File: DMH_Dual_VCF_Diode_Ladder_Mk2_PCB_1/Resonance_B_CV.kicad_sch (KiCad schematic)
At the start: 26 parts, among them J22 Conn_01x06_PinHeader, Q3 BC548, Q4 BC548, SW8 SW_DPDT_x2, U2 TL074

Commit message: Corrected pin header footprint assignments
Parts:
- J22: footprint Connector_PinHeader_2.54mm:PinHeader_1x10_P2.54mm_Vertical -> Connector_PinHeader_2.54mm:PinHeader_1x06_P2.54mm_Vertical
- J22: footprint (none) -> Connector_PinHeader_2.54mm:PinHeader_1x06_P2.54mm_Vertical
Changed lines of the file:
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@@
 			)
 		)
-		(property "Footprint" "Connector_PinHeader_2.54mm:PinHeader_1x10_P2.54mm_Vertical"
+		(property "Footprint" "Connector_PinHeader_2.54mm:PinHeader_1x06_P2.54mm_Vertical"
 			(at 76.2 100.33 0)
 			(effects
@@
 			)
 		)
-		(property "Footprint" ""
+		(property "Footprint" "Connector_PinHeader_2.54mm:PinHeader_1x06_P2.54mm_Vertical"
 			(at 170.18 132.08 0)
 			(effects
@@
 			)
 		)
-		(property "Footprint" ""
+		(property "Footprint" "Connector_PinHeader_2.54mm:PinHeader_1x06_P2.54mm_Vertical"
 			(at 165.1 113.03 0)
 			(effects
@@
 			)
 		)
-		(property "Footprint" "Connector_PinHeader_2.54mm:PinHeader_1x10_P2.54mm_Vertical"
+		(property "Footprint" "Connector_PinHeader_2.54mm:PinHeader_1x06_P2.54mm_Vertical"
 			(at 63.5 81.28 0)
 			(effects
@@
 			)
 		)
-		(property "Footprint" ""
+		(property "Footprint" "Connector_PinHeader_2.54mm:PinHeader_1x06_P2.54mm_Vertical"
 			(at 185.42 132.08 0)
 			(effects
@@
 			)
 		)
-		(property "Footprint" "Connector_PinHeader_2.54mm:PinHeader_1x10_P2.54mm_Vertical"
+		(property "Footprint" "Connector_PinHeader_2.54mm:PinHeader_1x06_P2.54mm_Vertical"
 			(at 110.49 129.54 0)
 			(effects

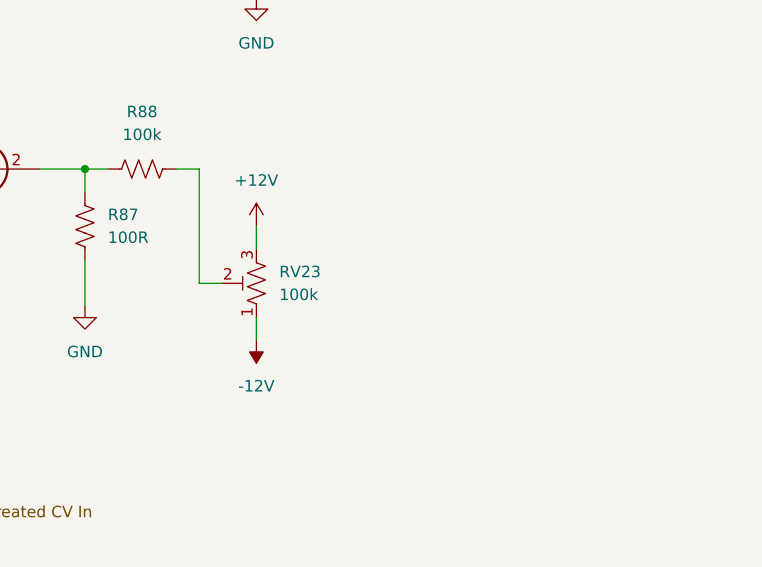
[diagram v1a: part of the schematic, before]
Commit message: Added trim pot functions to silkscreen
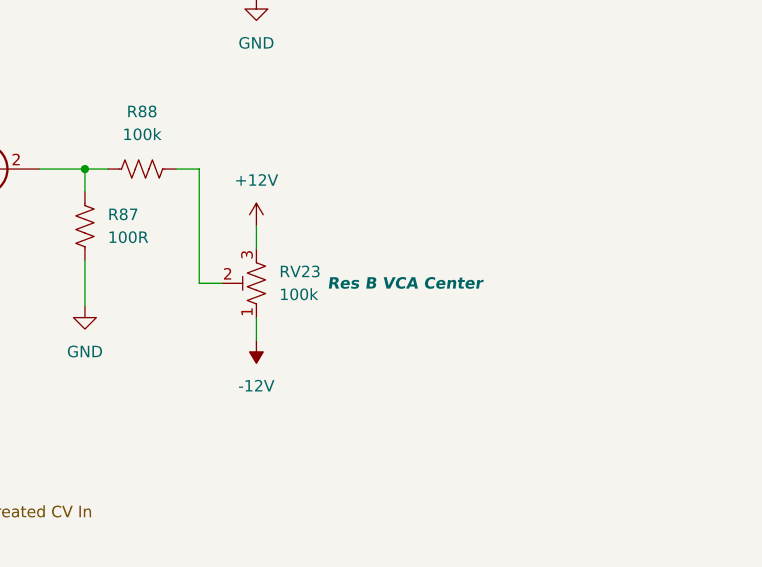
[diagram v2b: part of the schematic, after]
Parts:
- RV23: Function (none) -> Res B VCA Center
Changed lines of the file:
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@@
 		(on_board yes)
 		(dnp no)
-		(fields_autoplaced yes)
 		(property "Reference" "RV23"
 			(at 224.79 100.3299 0)
@@
 			)
 		)
+		(property "Function" "Res B VCA Center"
+			(at 238.76 101.6 0)
+			(effects
+				(font
+					(size 1.27 1.27)
+					(thickness 0.254)
+					(bold yes)
+					(italic yes)
+				)
+			)
+		)

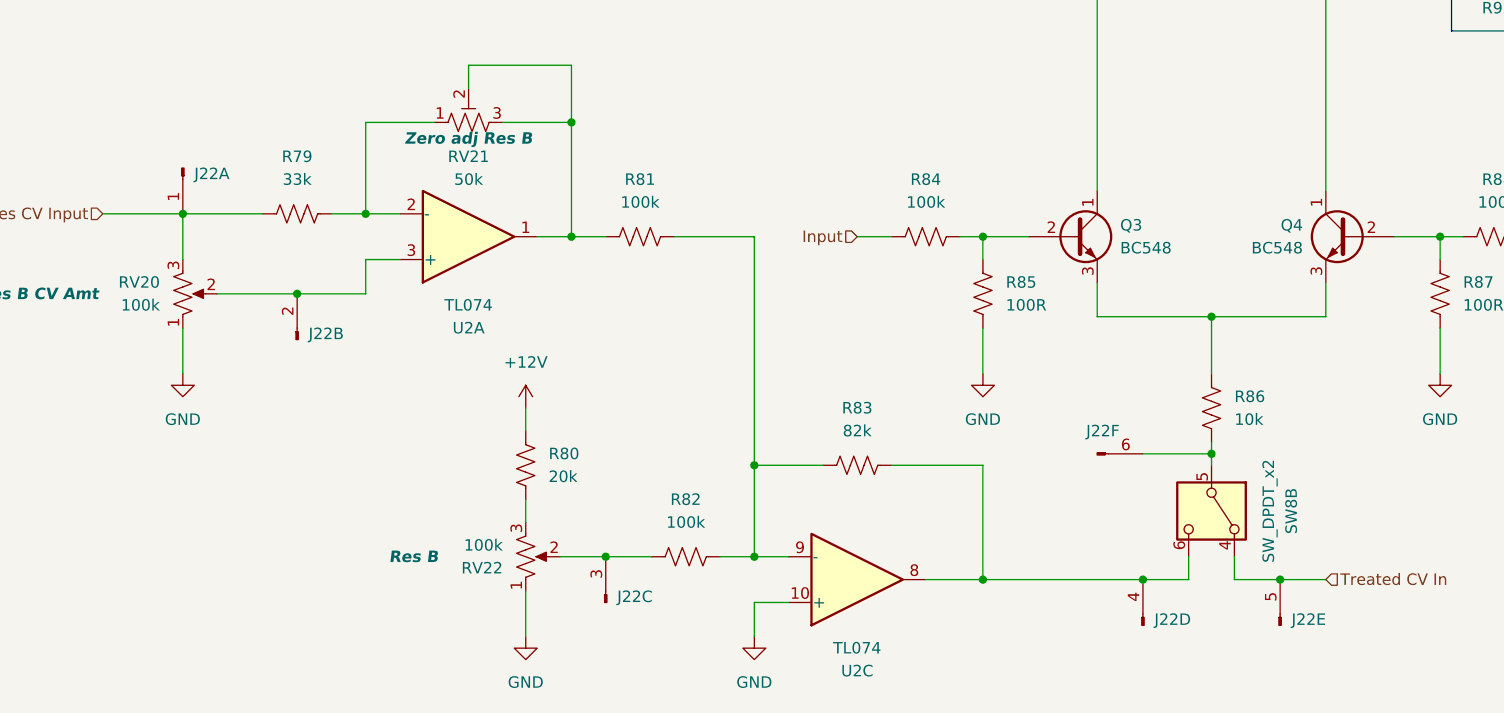
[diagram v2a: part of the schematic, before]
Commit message: Adjusted pin header connections
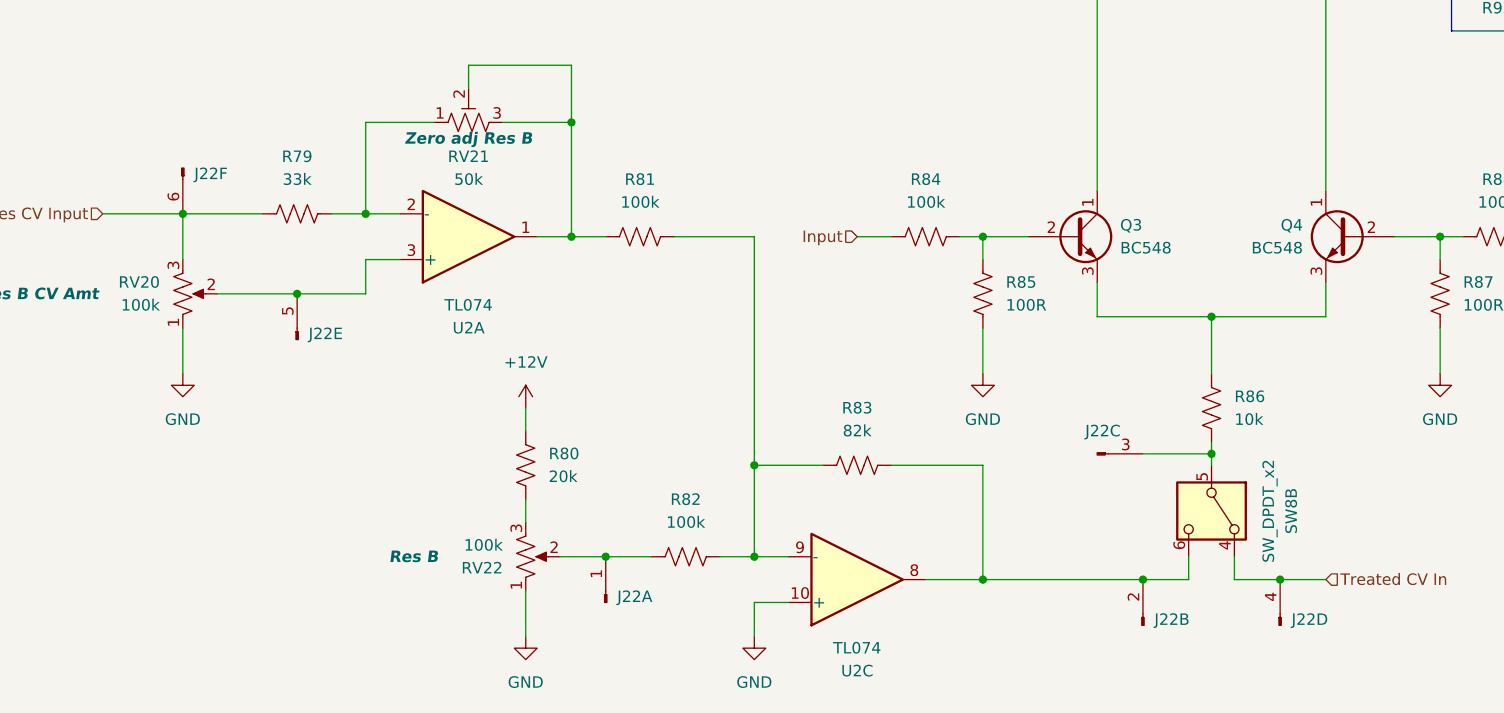
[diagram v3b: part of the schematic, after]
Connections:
- net Res CV Input: now also J22.6 (Pin_6); no longer J22.1 (Pin_1)
- net Treated CV In: now also J22.4 (Pin_4); no longer J22.5 (Pin_5)
- net at RV20.2, U2.3 (+): now also J22.5 (Pin_5); no longer J22.2 (Pin_2)
- net at R86.1, SW8.5 (B): now also J22.3 (Pin_3); no longer J22.6 (Pin_6)
- net at R83.2, SW8.6 (C), U2.8: now also J22.2 (Pin_2); no longer J22.4 (Pin_4)
- net at R82.1, RV22.2: now also J22.1 (Pin_1); no longer J22.3 (Pin_3)
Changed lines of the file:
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@@
 		(lib_id "SynthStuff:Conn_01x06_PinHeader")
 		(at 76.2 100.33 90)
-		(unit 2)
+		(unit 5)
 		(exclude_from_sim no)
 		(in_bom yes)
@@
 				(path "/58f4306d-5387-4983-bb08-41a2313fd315/f0045393-e1d0-4de8-baba-b9053cd8a11d"
 					(reference "J22")
-					(unit 2)
+					(unit 5)
 				)
 			)
@@
 		(lib_id "SynthStuff:Conn_01x06_PinHeader")
 		(at 170.18 132.08 90)
-		(unit 4)
+		(unit 2)
 		(exclude_from_sim no)
 		(in_bom yes)
@@
 			)
 		)
+		(property "Function" ""
+			(at 170.18 132.08 0)
+			(effects
+				(font
+					(size 1.27 1.27)
+				)
+			)
+		)
 		(pin "2"
 		)
@@
 				(path "/58f4306d-5387-4983-bb08-41a2313fd315/f0045393-e1d0-4de8-baba-b9053cd8a11d"
 					(reference "J22")
-					(unit 4)
+					(unit 2)
 				)
 			)
@@
 		(lib_id "SynthStuff:Conn_01x06_PinHeader")
 		(at 165.1 113.03 0)
-		(unit 6)
+		(unit 3)
 		(exclude_from_sim no)
 		(in_bom yes)
@@
 			)
 		)
+		(property "Function" ""
+			(at 165.1 113.03 0)
+			(effects
+				(font
+					(size 1.27 1.27)
+				)
+			)
+		)
 		(pin "2"
 		)
@@
 				(path "/58f4306d-5387-4983-bb08-41a2313fd315/f0045393-e1d0-4de8-baba-b9053cd8a11d"
 					(reference "J22")
-					(unit 6)
+					(unit 3)
 				)
 			)
@@
 		(lib_id "SynthStuff:Conn_01x06_PinHeader")
 		(at 63.5 81.28 270)
-		(unit 1)
+		(unit 6)
 		(exclude_from_sim no)
 		(in_bom yes)
@@
 				(path "/58f4306d-5387-4983-bb08-41a2313fd315/f0045393-e1d0-4de8-baba-b9053cd8a11d"
 					(reference "J22")
-					(unit 1)
+					(unit 6)
 				)
 			)
@@
 		(lib_id "SynthStuff:Conn_01x06_PinHeader")
 		(at 185.42 132.08 90)
-		(unit 5)
+		(unit 4)
 		(exclude_from_sim no)
 		(in_bom yes)
@@
 			)
 		)
+		(property "Function" ""
+			(at 185.42 132.08 0)
+			(effects
+				(font
+					(size 1.27 1.27)
+				)
+			)
+		)
 		(pin "2"
 		)
@@
 				(path "/58f4306d-5387-4983-bb08-41a2313fd315/f0045393-e1d0-4de8-baba-b9053cd8a11d"
 					(reference "J22")
-					(unit 5)
+					(unit 4)
 				)
 			)
@@
 		(lib_id "SynthStuff:Conn_01x06_PinHeader")
 		(at 110.49 129.54 90)
-		(unit 3)
+		(unit 1)
 		(exclude_from_sim no)
 		(in_bom yes)
@@
 				(path "/58f4306d-5387-4983-bb08-41a2313fd315/f0045393-e1d0-4de8-baba-b9053cd8a11d"
 					(reference "J22")
-					(unit 3)
-				)
-			)
+					(unit 1)
+				)
+			)

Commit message: Changed VCA CV summing stage feedback to 100k
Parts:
- R83: value 82k -> 100k
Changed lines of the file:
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@@
 			)
 		)
-		(property "Value" "82k"
+		(property "Value" "100k"
 			(at 138.43 110.49 90)
 			(effects

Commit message: Updated schematic during validation
- Changed Resonance B VCA gain resistors to 2k2
- Added range limiting resistors to all Cutoff pots
- Moved 48x gain to non-inverting opamp stage in Core Circuit to allow for Resonance voltage control.
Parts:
- R93, R94: value 100k -> 2k2
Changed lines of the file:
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@@
 			)
 		)
-		(property "Value" "100k"
+		(property "Value" "2k2"
 			(at 224.79 64.7699 0)
 			(effects
@@
 			)
 		)
-		(property "Value" "100k"
+		(property "Value" "2k2"
 			(at 234.95 34.29 90)
 			(effects

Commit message: Updated various resistor values
... and deleted all VCAs output 1k resistors
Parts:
- removed R95: 1k, Resistor_THT:R_Axial_DIN0207_L6.3mm_D2.5mm_P7.62mm_Horizontal, symbol Device:R_US
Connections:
- net Output: now also R94.1, U2.7
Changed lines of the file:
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@@
-	(wire
-		(pts
-			(xy 257.81 50.8) (xy 266.7 50.8)
-		)
-		(stroke
-			(width 0)
-			(type default)
-		)
-	)
 	(wire
 		(pts
@@
 	(wire
 		(pts
-			(xy 246.38 50.8) (xy 250.19 50.8)
+			(xy 246.38 50.8) (xy 266.7 50.8)
 		)
 		(stroke
@@
 				)
 			)
-		)
-	)
-	(symbol
-		(lib_id "Device:R_US")
-		(at 254 50.8 270)
-		(unit 1)
-		(exclude_from_sim no)
-		(in_bom yes)
-		(on_board yes)
-		(dnp no)
-		(fields_autoplaced yes)
-		(property "Reference" "R95"
-			(at 254 44.45 90)
-			(effects
-				(font
-					(size 1.27 1.27)
-				)
-			)
-		)
-		(property "Value" "1k"
-			(at 254 46.99 90)
-			(effects
-				(font
-					(size 1.27 1.27)
-				)
-			)
-		)
-		(property "Footprint" "Resistor_THT:R_Axial_DIN0207_L6.3mm_D2.5mm_P7.62mm_Horizontal"
-			(at 253.746 51.816 90)
-			(effects
-				(font
-					(size 1.27 1.27)
-				)
-				(hide yes)
-			)
-		)
-		(property "Datasheet" "~"
-			(at 254 50.8 0)
-			(effects
-				(font
-					(size 1.27 1.27)
-				)
-				(hide yes)
-			)
-		)
-		(property "Description" "Resistor, US symbol"
-			(at 254 50.8 0)
-			(effects
-				(font
-					(size 1.27 1.27)
-				)
-				(hide yes)
-			)
-		)
-		(property "Function" ""
-			(at 254 50.8 0)
-			(effects
-				(font
-					(size 1.27 1.27)
-				)
-			)
-		)
-		(pin "1"
-		)
-		(pin "2"
-		)
-		(instances
-			(project "DMH_Dual_VCF_Diode_Ladder_PCB"
-				(path "/58f4306d-5387-4983-bb08-41a2313fd315/f0045393-e1d0-4de8-baba-b9053cd8a11d"
-					(reference "R95")
-					(unit 1)
-				)
-			)
